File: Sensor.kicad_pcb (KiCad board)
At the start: 2 copper layers, 100 x 100 mm, 8 parts, among them J2 Barrel_Jack_Switch, U10 ATtiny1616-S, U11 SA39-11EWA, U12 SA39-11EWA, U13 SA39-11EWA, U2 LD1117S50TR_SOT223, U9 MCP9700Ax-ELT

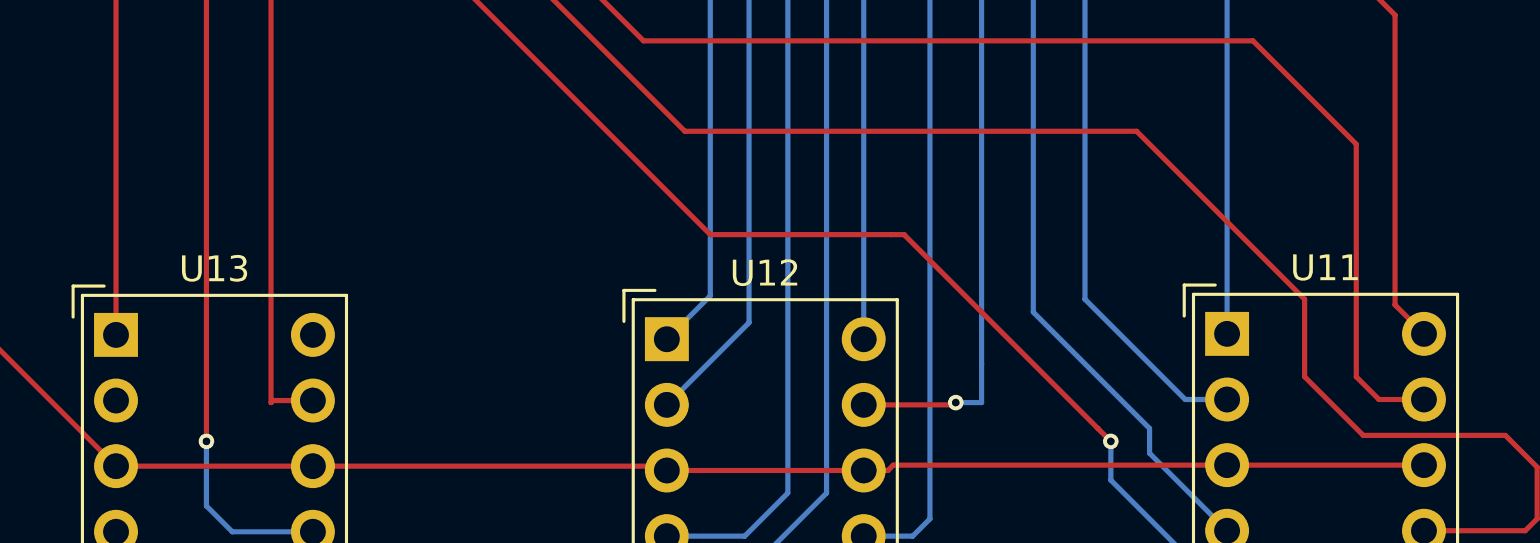
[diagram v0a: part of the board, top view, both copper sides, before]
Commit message: fix: change 7SEG label on chip
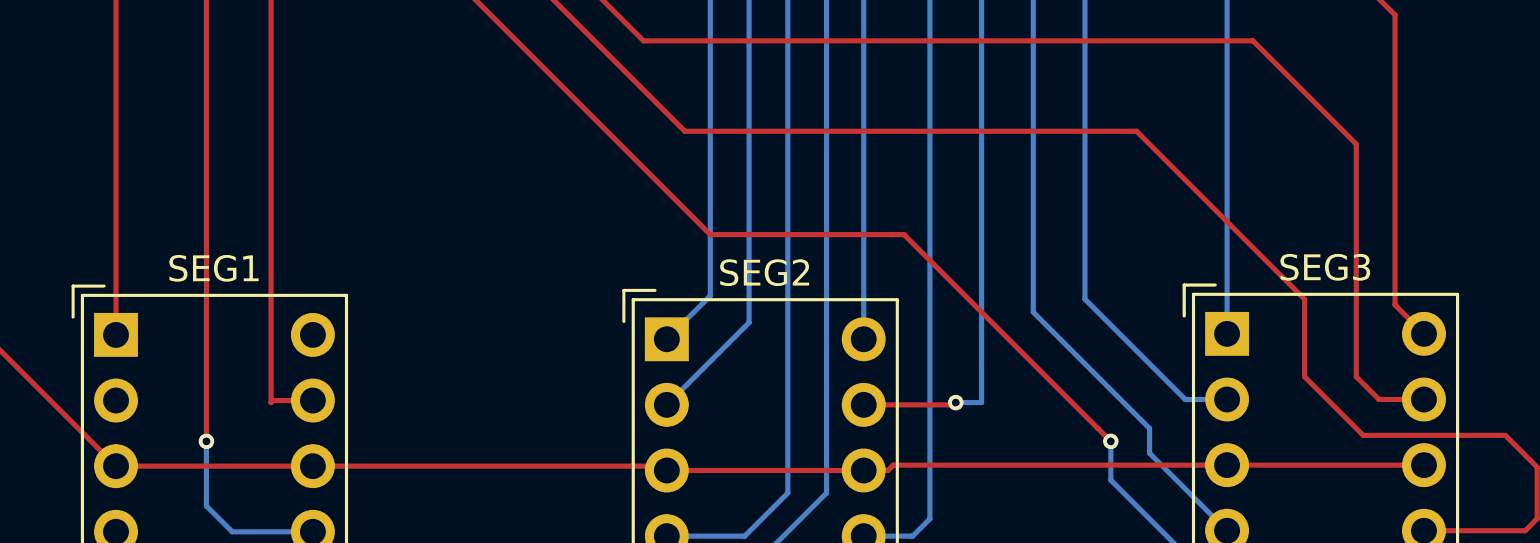
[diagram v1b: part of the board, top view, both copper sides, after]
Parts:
- renumbered U13 to SEG1, U12 to SEG2, U11 to SEG3
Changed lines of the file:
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@@
 		(descr "Single digit 7 segment LED display in red, yellow or green colour http://www.kingbrightusa.com/images/catalog/SPEC/sa39-11ewa.pdf")
 		(tags "One digit LED 7 segment SA39-11 SC39-11 SA39-12 SC39-12")
-		(property "Reference" "U11"
+		(property "Reference" "SEG3"
 			(at 3.81 -2.54 0)
 			(layer "F.SilkS")
@@
 		(descr "Single digit 7 segment LED display in red, yellow or green colour http://www.kingbrightusa.com/images/catalog/SPEC/sa39-11ewa.pdf")
 		(tags "One digit LED 7 segment SA39-11 SC39-11 SA39-12 SC39-12")
-		(property "Reference" "U12"
+		(property "Reference" "SEG2"
 			(at 3.81 -2.54 0)
 			(layer "F.SilkS")
@@
 		(descr "Single digit 7 segment LED display in red, yellow or green colour http://www.kingbrightusa.com/images/catalog/SPEC/sa39-11ewa.pdf")
 		(tags "One digit LED 7 segment SA39-11 SC39-11 SA39-12 SC39-12")
-		(property "Reference" "U13"
+		(property "Reference" "SEG1"
 			(at 3.81 -2.54 0)
 			(layer "F.SilkS")

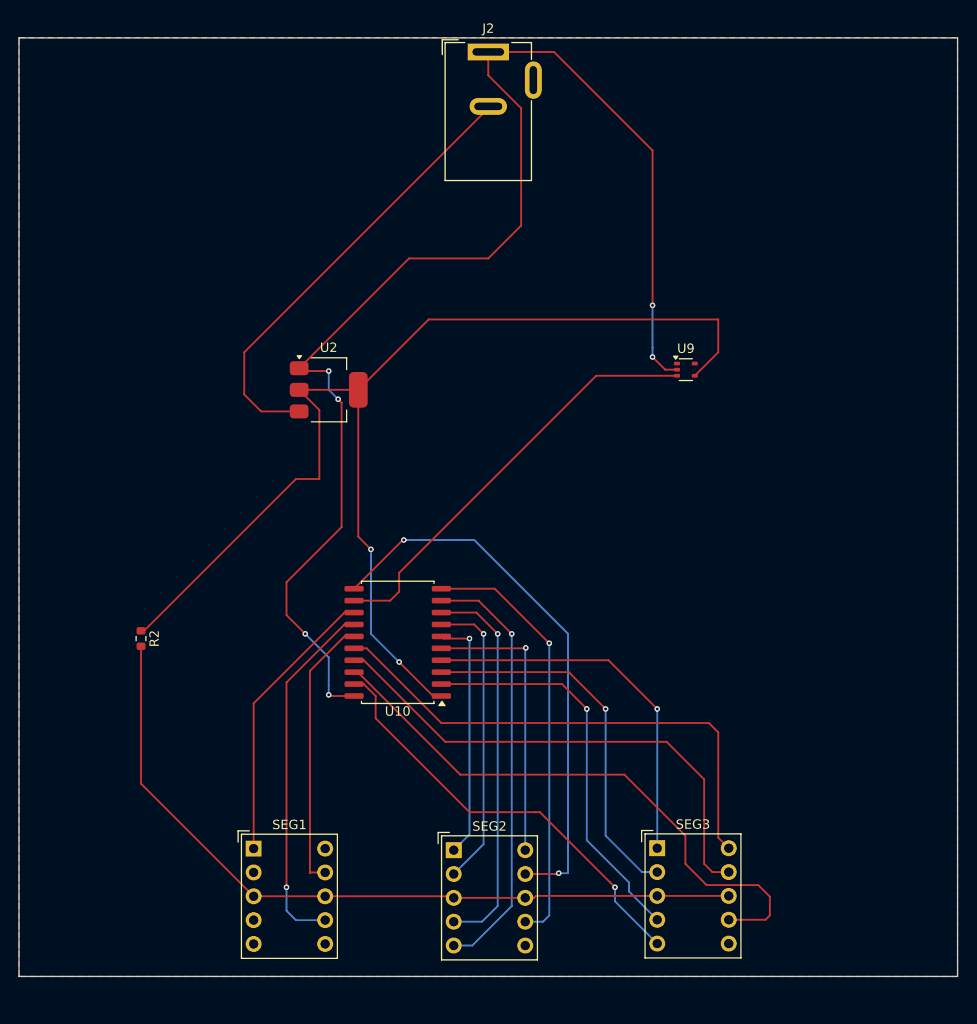
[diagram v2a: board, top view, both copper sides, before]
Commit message: fix: erc input/output errors
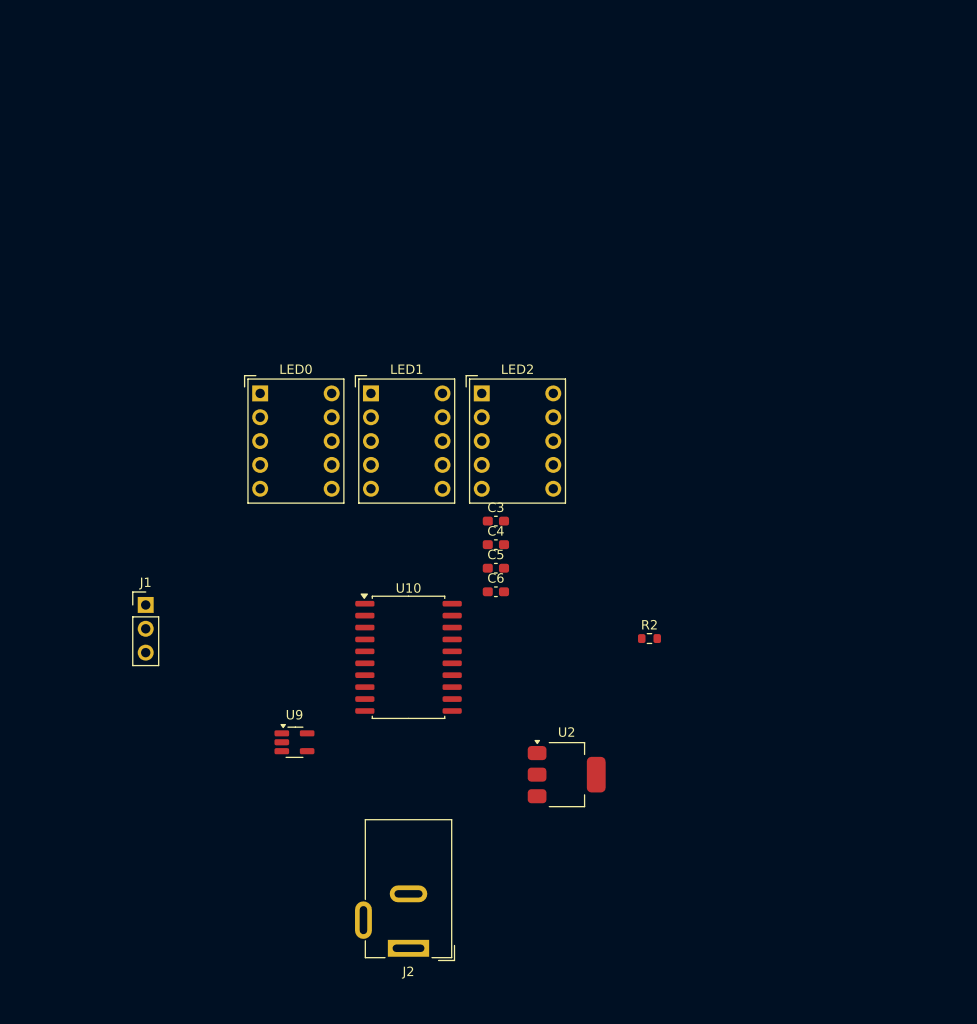
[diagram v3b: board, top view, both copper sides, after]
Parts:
- removed SEG1, SEG2, SEG3: SA39-11EWA, Display_7Segment:Sx39-1xxxxx
- added C3: 100nF, Capacitor_SMD:C_0603_1608Metric_Pad1.08x0.95mm_HandSolder, F.Cu at (150.8, 101.5)
- added C4: 100nF, Capacitor_SMD:C_0603_1608Metric_Pad1.08x0.95mm_HandSolder, F.Cu at (150.8, 104.0)
- added C5: 100nF, Capacitor_SMD:C_0603_1608Metric_Pad1.08x0.95mm_HandSolder, F.Cu at (150.8, 106.5)
- added C6: 100nF, Capacitor_SMD:C_0603_1608Metric_Pad1.08x0.95mm_HandSolder, F.Cu at (150.8, 109.0)
- added J1: ProgPins, Connector_PinHeader_2.54mm:PinHeader_1x03_P2.54mm_Vertical, F.Cu at (113.5, 110.4)
- added LED0: SA39-11EWA, Display_7Segment:Sx39-1xxxxx, F.Cu at (125.7, 87.9)
- added LED1: SA39-11EWA, Display_7Segment:Sx39-1xxxxx, F.Cu at (137.5, 87.9)
- added LED2: SA39-11EWA, Display_7Segment:Sx39-1xxxxx, F.Cu at (149.3, 87.9)
- J2: value Barrel_Jack_Switch -> Barrel
- R2: value 200 Ohms -> 150 Ohms
- U2: value LD1117S50TR_SOT223 -> LDO
- U9: footprint Package_TO_SOT_SMD:SOT-353_SC-70-5 -> Package_TO_SOT_SMD:SOT-23-5_HandSoldering
- moved J2 95.9 mm to (141.5, 147.0), turned to 180 degrees
- moved U9 57.6 mm to (129.3, 125.0)
- moved R2 54.2 mm to (167.2, 114.0), turned to 0 degrees
- moved U2 48.2 mm to (158.3, 128.5)
- moved U10 1.97 mm to (141.5, 116.0), turned to 0 degrees
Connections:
- R2 pad 1: Net-(U10-VCC) -> Net-(LED0-CA-Pad3)
- R2 pad 2: Net-(R2-Pad2) -> /5V
- U10 pad 10: Net-(U10-PB1) -> /SEG1-C
- U10 pad 11: Net-(U10-PB0) -> /SEG1-B
- U10 pad 12: Net-(U10-PC0) -> /SEG0-A
- U10 pad 13: Net-(U10-PC1) -> /SEG2-B
- U10 pad 14: Net-(U10-PC2) -> /SEG2-C
- U10 pad 15: Net-(U10-PC3) -> /SEG2-G
- U10 pad 16: Net-(U10-~{RESET}/PA0) -> Net-(J1-Pin_2)
- U10 pad 17: Net-(U10-PA1) -> /SEG0-B
- U10 pad 18: Net-(U10-PA2) -> /SEG0-C
- U10 pad 19: Net-(U10-PA3) -> /SEG0-D
- U10 pad 2: Net-(U10-PA4) -> /SEG0-E
- U10 pad 3: Net-(U10-PA5) -> /SEG0-F
- U10 pad 4: Net-(U10-PA6) -> /SEG0-G
- U10 pad 5: Net-(U10-PA7) -> /SEG1-A
- U10 pad 6: Net-(U10-PB5) -> /SEG1-G
- U10 pad 7: Net-(U10-PB4) -> /SEG1-F
- U10 pad 8: Net-(U10-PB3) -> /SEG1-E
- U10 pad 9: Net-(U10-PB2) -> /SEG1-D
- U2 pad 2: Net-(U10-VCC) -> Net-(U2-VO)
- U2 pad 3: VCC -> Net-(U2-VI)
- U9 pad 3: Net-(U10-PC0) -> Net-(J1-Pin_2)
- U9 pad 4: Net-(U10-VCC) -> Net-(U9-V_{DD})
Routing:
- net GND: track 142.3 -> 0.00 mm, vias 6 -> 0
- net Net-(U10-VCC): track 127.7 -> 0.00 mm, vias 2 -> 0
- net Net-(R2-Pad2): track 82.4 -> 0.00 mm
- net Net-(U10-PA2): track 62.5 -> 0.00 mm
- net Net-(U10-PB0): track 59.2 -> 0.00 mm, vias 2 -> 0
- net Net-(U10-~{RESET}/PA0): track 55.3 -> 0.00 mm
- net Net-(U10-PA1): track 54.5 -> 0.00 mm
- net VCC: track 48.1 -> 0.00 mm
- net Net-(U10-PA3): track 46.0 -> 0.00 mm, vias 1 -> 0
- net Net-(U10-PB2): track 45.9 -> 0.00 mm, vias 1 -> 0
- net Net-(U10-PB1): track 45.7 -> 0.00 mm, vias 1 -> 0
- net Net-(U10-PC0): track 45.5 -> 0.00 mm
- net Net-(U10-PA4): track 42.2 -> 0.00 mm, vias 1 -> 0
- net Net-(U10-PB3): track 41.3 -> 0.00 mm, vias 1 -> 0
- net Net-(U10-PA6): track 40.0 -> 0.00 mm, vias 1 -> 0
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- removed copper zone on F.Cu, net GND
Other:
- board outline removed

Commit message: feat: finished pcb
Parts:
- J1: value ProgPins -> Attiny1616 Programmer
- R2: value 150 Ohms -> 150Ω
- Volt. Reg: renamed from U2
- moved J1 56.1 mm to (169.5, 112.9)
- moved C5 34.5 mm to (156.5, 140.5), turned to 90 degrees
- moved C4 31.2 mm to (133.6, 130.0), turned to 180 degrees
- moved C3 26.5 mm to (142.0, 126.5), turned to 180 degrees
- moved C6 21.0 mm to (149.5, 130.0), turned to 180 degrees
- moved R2 16.5 mm to (165.0, 97.7), turned to -90 degrees
- moved Thermistor 4.74 mm to (126.2, 128.6)
- moved J2 2.55 mm to (141.0, 149.5)
- moved LED1 1.41 mm to (137.2, 86.5)
- moved LED2 1.41 mm to (149.0, 86.5)
- moved LED0 1.41 mm to (125.4, 86.5)
- moved Volt. Reg 1.15 mm to (159.5, 128.5)
- renumbered U10 to Attiny1616, U9 to Thermistor
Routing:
- net GND: track 0.00 -> 127.1 mm, vias 0 -> 14
- net /5V: track 0.00 -> 91.9 mm
- net Net-(LED0-CA-Pad3): track 0.00 -> 89.0 mm
- net Net-(J1-Pin_2): track 0.00 -> 62.2 mm, vias 0 -> 2
- net /SEG1-E: track 0.00 -> 58.6 mm, vias 0 -> 1
- net /SEG1-F: track 0.00 -> 56.4 mm, vias 0 -> 1
- net /SEG1-G: track 0.00 -> 54.7 mm, vias 0 -> 1
- net /SEG0-A: track 0.00 -> 43.5 mm
- net /SEG1-B: track 0.00 -> 36.4 mm, vias 0 -> 1
- net /SEG1-A: track 0.00 -> 36.3 mm, vias 0 -> 2
- net /SEG0-G: track 0.00 -> 35.9 mm
- net /SEG2-B: track 0.00 -> 35.5 mm, vias 0 -> 2
- net /SEG2-G: track 0.00 -> 33.4 mm
- net /SEG0-B: track 0.00 -> 33.4 mm
- net /SEG1-C: track 0.00 -> 33.3 mm, vias 0 -> 1
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- added copper zone on B.Cu, net GND
- added copper zone on F.Cu, net GND
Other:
- board outline added: 60 x 70 mm

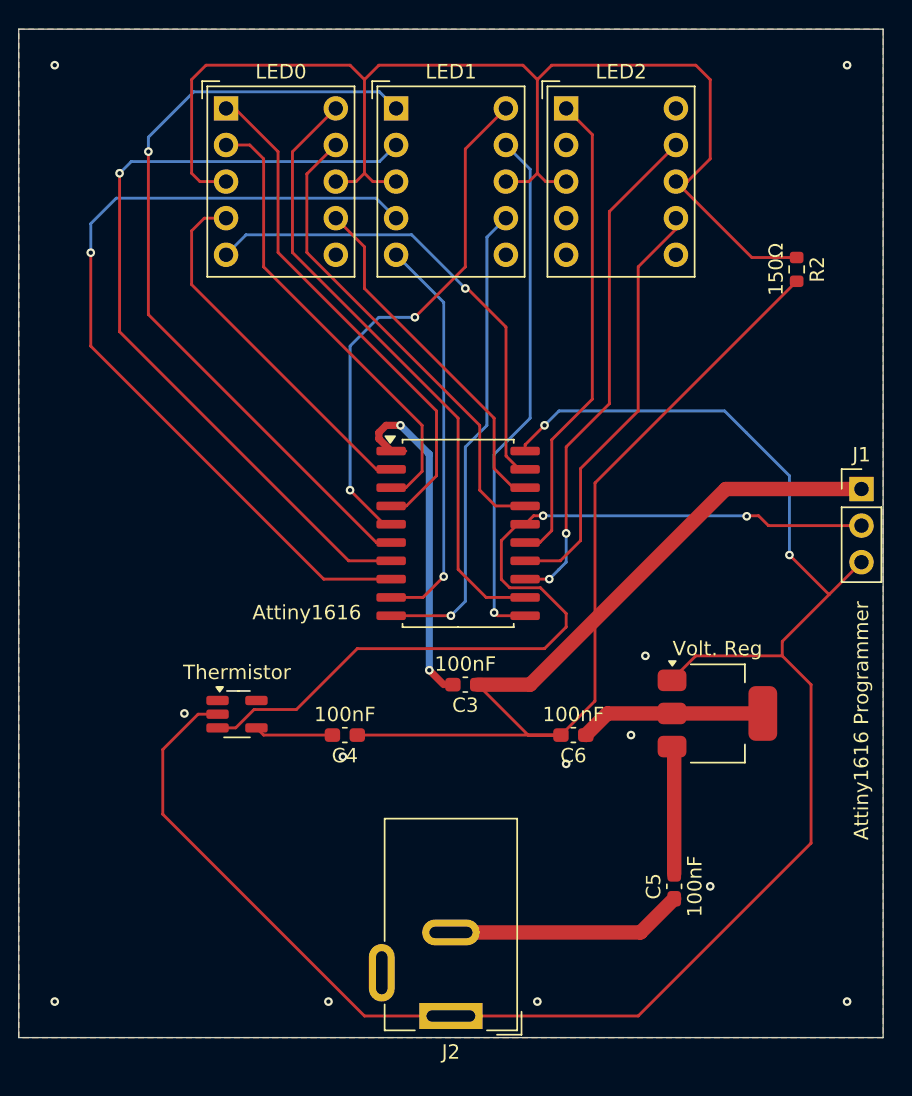
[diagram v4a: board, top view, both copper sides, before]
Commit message: fix: swapping leds 0 and 2 (units and sign/hundreds)
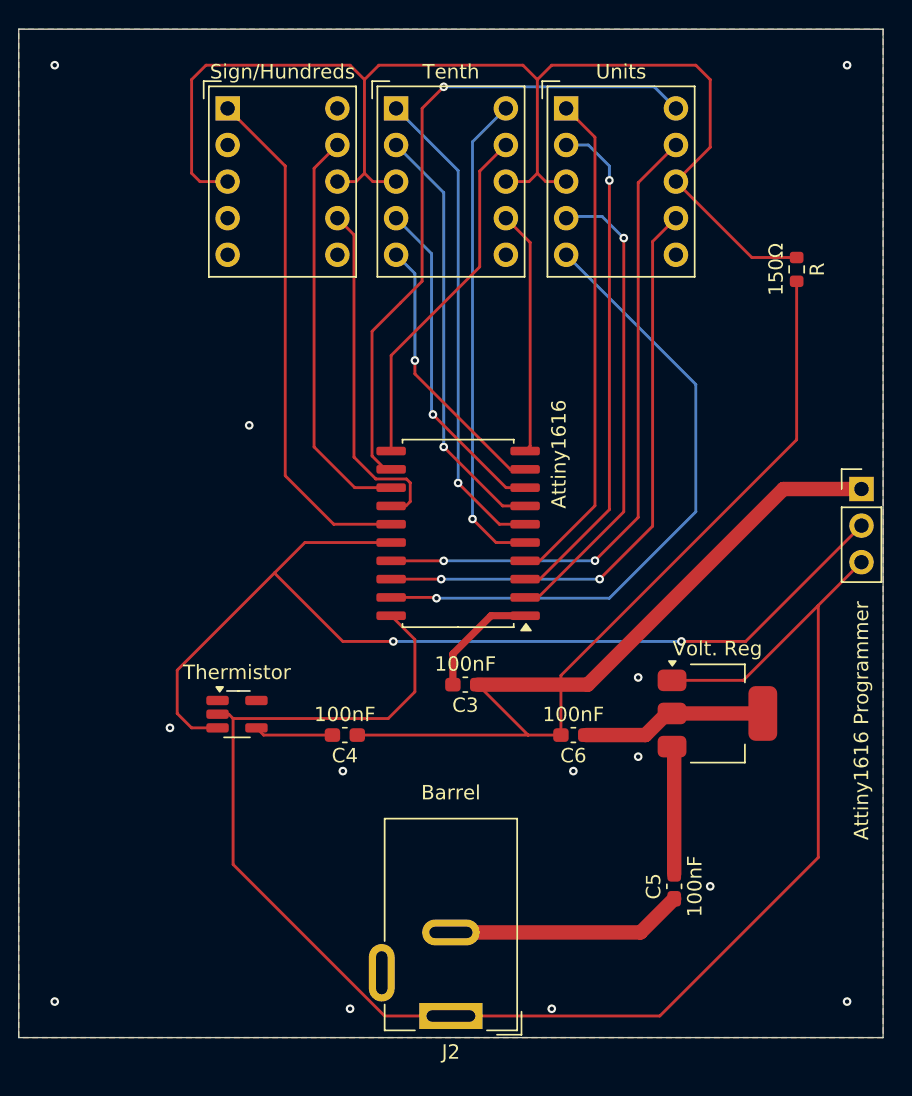
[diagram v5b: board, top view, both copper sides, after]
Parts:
- moved Units 23.6 mm to (149.0, 86.5)
- moved Sign/Hundreds 23.5 mm to (125.5, 86.5)
- turned Attiny1616 to 180 degrees
- renumbered R2 to R, LED2 to Sign/Hundreds, LED1 to Tenth, LED0 to Units
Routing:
- net /SEG1-E: track 58.6 -> 23.2 mm
- net /SEG1-F: track 56.4 -> 29.7 mm
- net /SEG1-G: track 54.7 -> 33.6 mm
- net /SEG0-C: track 24.6 -> 41.7 mm, vias 0 -> 2
- net /SEG1-C: track 33.3 -> 17.0 mm, vias 1 -> 0
- net Net-(U10-VCC): track 24.2 -> 8.47 mm, vias 2 -> 0
- net GND: track 127.1 -> 114.3 mm, vias 14 -> 13
- net /SEG0-B: track 33.4 -> 45.3 mm, vias 0 -> 2
- net /SEG0-D: track 33.3 -> 45.2 mm
- net /SEG1-B: track 36.4 -> 24.5 mm, vias 1 -> 0
- net /SEG1-D: track 28.0 -> 19.2 mm
- net Net-(J1-Pin_2): track 62.2 -> 70.8 mm
- net /SEG0-E: track 25.6 -> 33.0 mm, vias 0 -> 1
- net /SEG2-B: track 35.5 -> 28.2 mm, vias 2 -> 0
- net /SEG2-C: track 29.6 -> 24.5 mm
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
